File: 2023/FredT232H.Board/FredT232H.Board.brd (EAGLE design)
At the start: 88 x 77 mm, 17 parts

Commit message: Board 2023 fix first bug
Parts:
- moved LED_G_0 18.0 mm to (20.5, 47.0)
- moved LED_G_7 17.0 mm to (38.1, 47.0)
- moved LED_G_1 13.0 mm to (23.0, 47.0)
- moved LED_G_6 12.0 mm to (35.5, 47.0)
- moved LED_G_2 8.00 mm to (25.5, 47.0)
- moved LED_G_5 7.00 mm to (33.0, 47.0)
- moved LED_G_3 3.00 mm to (28.0, 47.0)
- moved LED_G_4 2.00 mm to (30.5, 47.0)
- moved GPIO_OUT 0.15 mm to (26.2, 15.3), turned to 180 degrees
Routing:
- net GND: track 233.4 -> 0.00 mm, vias 2 -> 0
- net VCC_33: track 168.6 -> 0.00 mm
- net D3_CS0: track 144.7 -> 0.00 mm
- net D4_CS1: track 108.8 -> 0.00 mm, vias 1 -> 0
- net D1_MOSI: track 107.8 -> 0.00 mm
- net D7_CS4: track 107.1 -> 0.00 mm, vias 1 -> 0
- net C4: track 105.8 -> 0.00 mm
- net D5_CS2: track 105.2 -> 0.00 mm, vias 1 -> 0
- net C7: track 103.8 -> 0.00 mm
- net D6_CS3: track 101.3 -> 0.00 mm, vias 2 -> 0
- net D2_MISO: track 99.5 -> 0.00 mm, vias 1 -> 0
- net D0_SCLK: track 98.9 -> 0.00 mm
- net C6: track 98.3 -> 0.00 mm
- net C5: track 92.8 -> 0.00 mm
- net C3: track 82.2 -> 0.00 mm
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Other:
- board text added: "PCBv2 - 2023.03"
- board text removed: "PCBv1 - 2023.02"

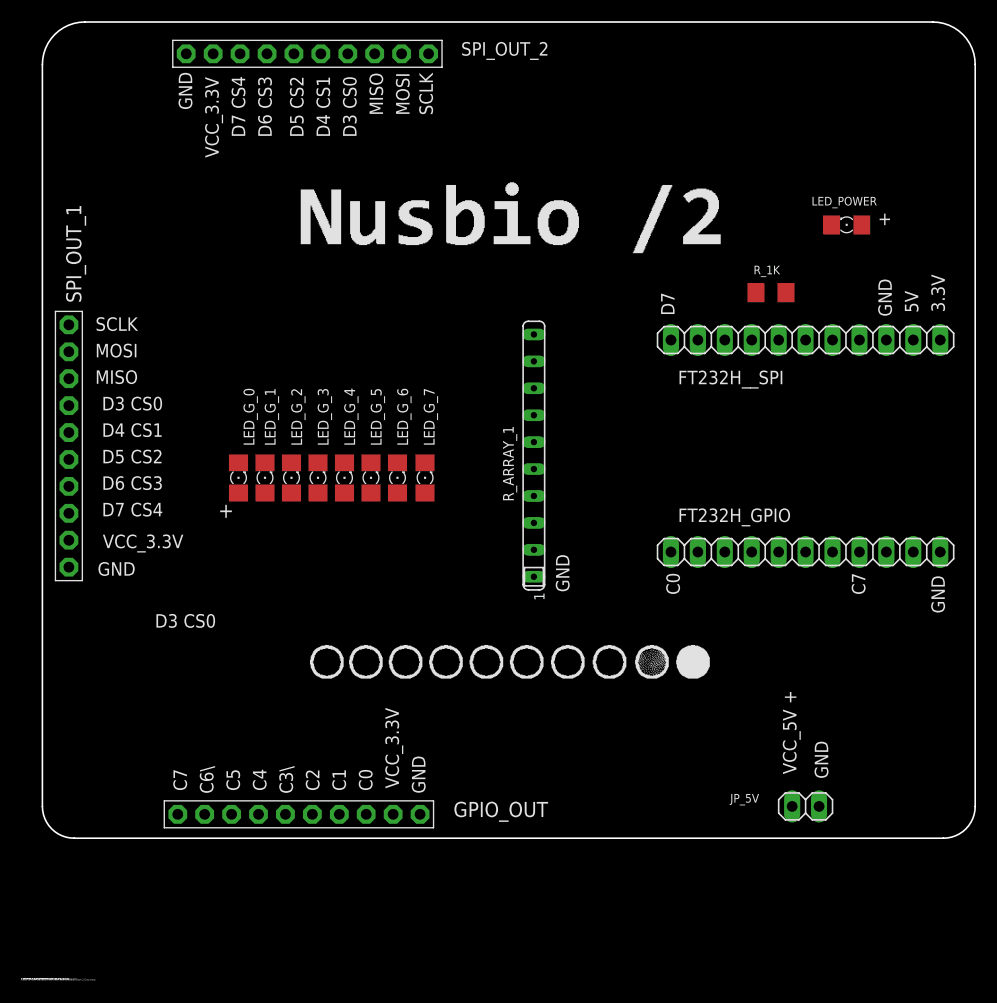
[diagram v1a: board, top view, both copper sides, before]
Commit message: Add pull up resistor to ft232h and i2c out 2
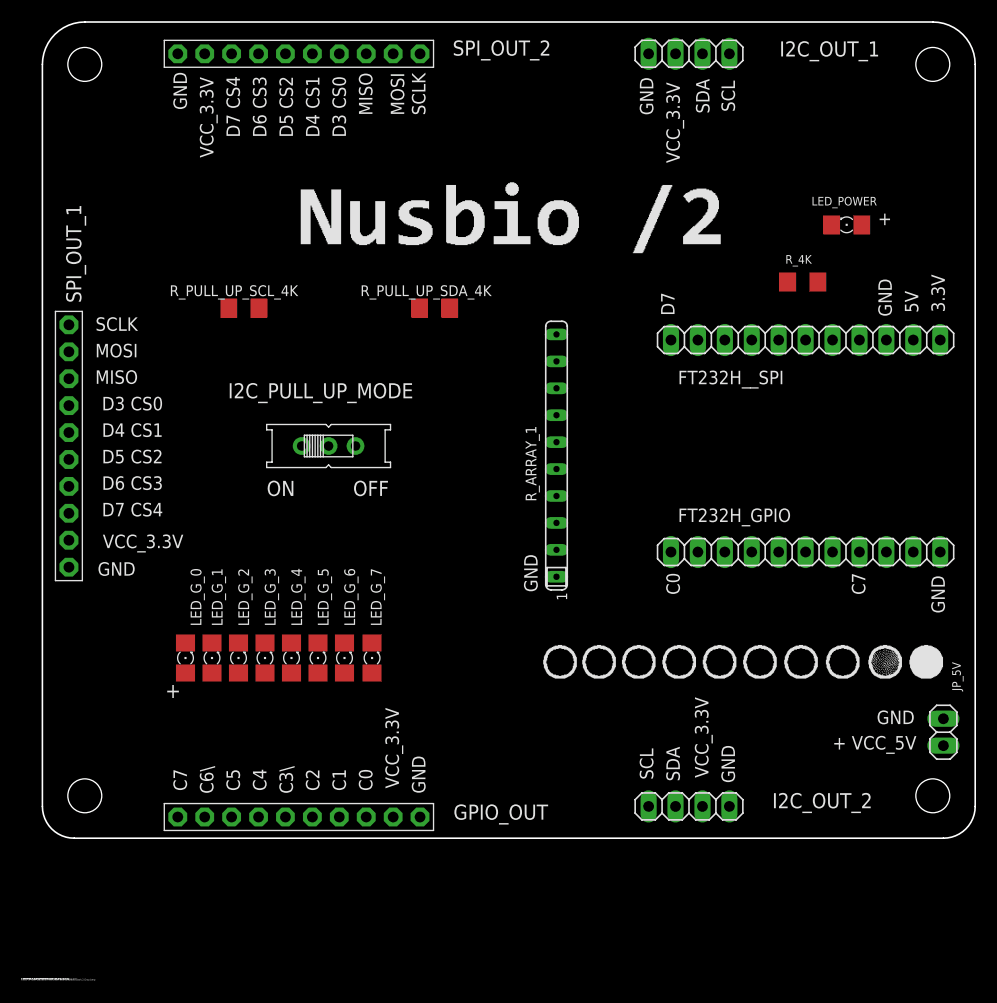
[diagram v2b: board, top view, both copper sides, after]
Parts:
- removed R_1K: (no value), adafruit:R1206
- added I2C_OUT_1, I2C_OUT_2: (no value), pinhead:1X04
- added I2C_PULL_UP_MODE: (no value), adafruit:EG1218
- added R_4K, R_PULL_UP_SCL_4K, R_PULL_UP_SDA_4K: (no value), adafruit:R1206
- moved LED_G_0 17.7 mm to (15.5, 30.0)
- moved LED_G_1 17.7 mm to (18.0, 30.0)
- moved LED_G_2 17.7 mm to (20.5, 30.0)
- moved LED_G_3 17.7 mm to (23.0, 30.0)
- moved LED_G_4 17.7 mm to (25.5, 30.0)
- moved LED_G_5 17.7 mm to (28.0, 30.0)
- moved LED_G_6 17.7 mm to (30.5, 30.0)
- moved LED_G_7 17.7 mm to (33.1, 30.0)
- moved JP_5V 14.8 mm to (87.0, 23.0), turned to 270 degrees
- moved R_ARRAY_1 2.13 mm to (50.5, 49.1)
- moved SPI_OUT_2 0.80 mm to (26.2, 87.0)
- moved GPIO_OUT 0.25 mm to (26.2, 15.0)
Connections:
- new net N$2: I2C_PULL_UP_MODE.O, R_PULL_UP_SCL_4K.2, R_PULL_UP_SDA_4K.2
- net D0_SCLK: now also I2C_OUT_1.1, I2C_OUT_2.1, R_PULL_UP_SCL_4K.1
- net D1_MOSI: now also R_PULL_UP_SDA_4K.1
- net D2_MISO: now also I2C_OUT_1.2, I2C_OUT_2.2
- net GND: now also I2C_OUT_1.4, I2C_OUT_2.4, R_4K.1; no longer R_1K.1
- net N$1: now also R_4K.2; no longer R_1K.2
- net VCC_33: now also I2C_OUT_1.3, I2C_OUT_2.3, I2C_PULL_UP_MODE.P
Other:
- board text added: "+ VCC_5V"
- board text added: "OFF"
- board text added: "ON"
- board text added: "SCL"
- board text added: "SDA"
- board text removed: "VCC_5V +"

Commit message: More on FT232 board
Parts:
- added H1, H2, H3, H4: MOUNT-PAD-ROUND3.3, holes:3,3-PAD
- added I2C_DTA_CONN: (no value), adafruit:EG1218
- moved JP_5V 53.0 mm to (87.0, 76.0)
- moved R_ARRAY_1 24.2 mm to (26.5, 52.1), turned to 270 degrees
- moved R_PULL_UP_SDA_4K 22.1 mm to (17.0, 65.0)
- moved I2C_PULL_UP_MODE 16.5 mm to (45.0, 54.0)
- moved R_PULL_UP_SCL_4K 16.1 mm to (37.0, 65.0)
- moved LED_G_0 4.24 mm to (18.5, 27.0)
- moved LED_G_1 4.24 mm to (21.0, 27.0)
- moved LED_G_2 4.24 mm to (23.5, 27.0)
- moved LED_G_3 4.24 mm to (26.0, 27.0)
- moved LED_G_4 4.24 mm to (28.5, 27.0)
- moved LED_G_5 4.24 mm to (31.0, 27.0)
- moved LED_G_6 4.24 mm to (33.5, 27.0)
- moved LED_G_7 4.24 mm to (36.1, 27.0)
- moved LED_POWER 2.00 mm to (75.9, 70.9)
- moved GPIO_OUT 0.50 mm to (26.2, 15.5)
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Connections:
- net D1_MOSI: now also I2C_DTA_CONN.P
- net D2_MISO: now also I2C_DTA_CONN.O
- net GND: now also H1.B3,3, H2.B3,3, H3.B3,3, H4.B3,3
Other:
- board text added: "VCC_3V"

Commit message: More on FT232 board
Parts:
- moved JP_5V 94.0 mm to (5.00, 30.0)
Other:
- board text added: "VCC_5V"
- board text removed: "+ VCC_5V"
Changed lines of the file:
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@@
 <text x="37.5" y="19" size="1.27" layer="25" rot="R90" align="center">GND</text>
 <text x="35" y="20.7" size="1.27" layer="25" rot="R90" align="center">VCC_3V</text>
-<text x="32.5" y="18.5" size="1.27" layer="25" rot="R90" align="center">C0</text>
-<text x="30" y="18.5" size="1.27" layer="25" rot="R90" align="center">C1</text>
-<text x="27.5" y="18.5" size="1.27" layer="25" rot="R90" align="center">C2</text>
-<text x="25" y="18.5" size="1.27" layer="25" rot="R90" align="center">C3\</text>
-<text x="22.5" y="18.5" size="1.27" layer="25" rot="R90" align="center">C4</text>
-<text x="20" y="18.5" size="1.27" layer="25" rot="R90" align="center">C5</text>
-<text x="17.5" y="18.5" size="1.27" layer="25" rot="R90" align="center">C6\</text>
-<text x="15" y="18.5" size="1.27" layer="25" rot="R90" align="center">C7</text>
+<text x="14.7" y="18.5" size="1.27" layer="25" rot="R90" align="center">C0</text>
+<text x="17.2" y="18.5" size="1.27" layer="25" rot="R90" align="center">C1</text>
+<text x="19.7" y="18.5" size="1.27" layer="25" rot="R90" align="center">C2</text>
+<text x="22.2" y="18.5" size="1.27" layer="25" rot="R90" align="center">C3\</text>
+<text x="24.8" y="18.5" size="1.27" layer="25" rot="R90" align="center">C4</text>
+<text x="27.5" y="18.5" size="1.27" layer="25" rot="R90" align="center">C5</text>
+<text x="30" y="18.5" size="1.27" layer="25" rot="R90" align="center">C6\</text>
+<text x="32.5" y="18.5" size="1.27" layer="25" rot="R90" align="center">C7</text>
 <text x="17.3255" y="23.939" size="1.4224" layer="25" rot="R180" align="center">+</text>
 <text x="0" y="-0.3175" size="0.127" layer="25" font="vector">C:/DVT/Fred.PCB/2023/MadeInTheUSB.Logo.Gray.50.bmp</text>
@@
 <text x="24.084" y="40.002" size="1.27" layer="25" rot="R90" align="center">GND</text>
 <text x="79" y="37" size="1.27" layer="25" rot="R270" align="center">C7</text>
-<text x="80.5" y="75" size="1.27" layer="25" align="center">+ VCC_5V</text>
-<text x="82.5" y="77.4" size="1.27" layer="25" align="center">GND</text>
+<text x="11" y="28.5" size="1.27" layer="25" align="center">VCC_5V</text>
+<text x="9.5" y="31.4" size="1.27" layer="25" align="center">GND</text>
 <text x="15" y="83.5" size="1.27" layer="25" rot="R90" align="center">GND</text>
 <text x="17.5" y="81" size="1.27" layer="25" rot="R90" align="center">VCC_3.3V</text>
@@
 <attribute name="VALUE" x="14.77" y="83.825" size="1.27" layer="27"/>
 </element>
-<element name="JP_5V" library="pinhead" library_urn="urn:adsk.eagle:library:325" package="1X02" package3d_urn="urn:adsk.eagle:package:22435/2" value="" x="87" y="76" smashed="yes" rot="R270">
-<attribute name="NAME" x="86.8288" y="72.6162" size="0.8128" layer="25" ratio="10" rot="R270"/>
-<attribute name="POPULARITY" value="98" x="87" y="76" size="1.778" layer="27" rot="R270" display="off"/>
-<attribute name="VALUE" x="83.825" y="78.54" size="1.27" layer="27" rot="R270"/>
+<element name="JP_5V" library="pinhead" library_urn="urn:adsk.eagle:library:325" package="1X02" package3d_urn="urn:adsk.eagle:package:22435/2" value="" x="5" y="30" smashed="yes" rot="R270">
+<attribute name="NAME" x="3.5" y="26" size="0.8128" layer="25" ratio="10"/>
+<attribute name="POPULARITY" value="98" x="5" y="30" size="1.778" layer="27" rot="R270" display="off"/>
+<attribute name="VALUE" x="1.825" y="32.54" size="1.27" layer="27" rot="R270"/>
 </element>
 <element name="I2C_OUT_1" library="pinhead" library_urn="urn:adsk.eagle:library:325" package="1X04" package3d_urn="urn:adsk.eagle:package:22407/2" value="" x="63" y="87" smashed="yes" rot="R180">
@@
 <contactref element="H3" pad="B3,3"/>
 <contactref element="H4" pad="B3,3"/>
-<wire x1="87" y1="77.27" x2="84" y2="84" width="0" layer="19" extent="1-1"/>
-<wire x1="81.62" y1="60" x2="87" y2="77.27" width="0" layer="19" extent="1-1"/>
-<wire x1="72.308" y1="65" x2="81.62" y2="60" width="0" layer="19" extent="1-1"/>
+<wire x1="72.308" y1="65" x2="84" y2="84" width="0" layer="19" extent="1-1"/>
+<wire x1="81.62" y1="60" x2="72.308" y2="65" width="0" layer="19" extent="1-1"/>
 <wire x1="86.7" y1="40" x2="81.62" y2="60" width="0" layer="19" extent="1-1"/>
 <wire x1="84" y1="19" x2="86.7" y2="40" width="0" layer="19" extent="1-1"/>
@@
 <wire x1="37.63" y1="15.5" x2="66.81" y2="15.5" width="0" layer="19" extent="1-1"/>
 <wire x1="8" y1="19" x2="37.63" y2="15.5" width="0" layer="19" extent="1-1"/>
-<wire x1="4.5" y1="38.57" x2="8" y2="19" width="0" layer="19" extent="1-1"/>
+<wire x1="5" y1="31.27" x2="8" y2="19" width="0" layer="19" extent="1-1"/>
+<wire x1="4.5" y1="38.57" x2="5" y2="31.27" width="0" layer="19" extent="1-1"/>
 <wire x1="26.5" y1="63.585" x2="4.5" y2="38.57" width="0" layer="19" extent="1-1"/>
 <wire x1="14.77" y1="87" x2="26.5" y2="63.585" width="0" layer="19" extent="1-1"/>
@@
 <contactref element="I2C_PULL_UP_MODE" pad="P"/>
 <contactref element="I2C_OUT_2" pad="3"/>
+<wire x1="86.7" y1="60" x2="61.73" y2="87" width="0" layer="19" extent="1-1"/>
 <wire x1="45" y1="54" x2="61.73" y2="87" width="0" layer="19" extent="1-1"/>
-<wire x1="86.7" y1="60" x2="61.73" y2="87" width="0" layer="19" extent="1-1"/>
 <wire x1="35.09" y1="15.5" x2="45" y2="54" width="0" layer="19" extent="1-1"/>
 <wire x1="64.27" y1="15.5" x2="35.09" y2="15.5" width="0" layer="19" extent="1-1"/>
@@
 <contactref element="LED_POWER" pad="A"/>
 <contactref element="JP_5V" pad="2"/>
-<wire x1="77.298134375" y1="70.86644375" x2="87" y2="74.73" width="0" layer="19" extent="1-1"/>
 <wire x1="84.16" y1="60" x2="77.298134375" y2="70.86644375" width="0" layer="19" extent="1-1"/>
+<wire x1="5" y1="28.73" x2="77.298134375" y2="70.86644375" width="0" layer="19" extent="1-1"/>
 </signal>
 <signal name="D0_SCLK">
@@
 <wire x1="37.63" y1="87" x2="66.81" y2="87" width="0" layer="19" extent="1-1"/>
 <wire x1="35.578" y1="65" x2="37.63" y2="87" width="0" layer="19" extent="1-1"/>
+<wire x1="79.08" y1="60" x2="66.81" y2="87" width="0" layer="19" extent="1-1"/>
 <wire x1="4.5" y1="61.43" x2="35.578" y2="65" width="0" layer="19" extent="1-1"/>
-<wire x1="79.08" y1="60" x2="66.81" y2="87" width="0" layer="19" extent="1-1"/>
 <wire x1="59.19" y1="15.5" x2="79.08" y2="60" width="0" layer="19" extent="1-1"/>
 </signal>
@@
 <wire x1="45" y1="44.5" x2="76.54" y2="60" width="0" layer="19" extent="1-1"/>
 <wire x1="15.578" y1="65" x2="45" y2="44.5" width="0" layer="19" extent="1-1"/>
+<wire x1="4.5" y1="58.89" x2="15.578" y2="65" width="0" layer="19" extent="1-1"/>
 <wire x1="35.09" y1="87" x2="15.578" y2="65" width="0" layer="19" extent="1-1"/>
-<wire x1="4.5" y1="58.89" x2="15.578" y2="65" width="0" layer="19" extent="1-1"/>
 </signal>
 <signal name="D2_MISO">
@@
 <contactref element="R_ARRAY_1" pad="8"/>
 <contactref element="LED_G_6" pad="C"/>
-<wire x1="26.5" y1="45.805" x2="33.5" y2="28.422" width="0" layer="19" extent="1-1"/>
+<wire x1="33.5" y1="28.422" x2="26.5" y2="45.805" width="0" layer="19" extent="1-1"/>
 </signal>
 <signal name="R_G_7">
 <contactref element="R_ARRAY_1" pad="9"/>
 <contactref element="LED_G_7" pad="C"/>
-<wire x1="26.5" y1="43.265" x2="36.101209375" y2="28.422" width="0" layer="19" extent="1-1"/>
+<wire x1="36.101209375" y1="28.422" x2="26.5" y2="43.265" width="0" layer="19" extent="1-1"/>
 </signal>
 <signal name="N$2">
@@
 <contactref element="R_PULL_UP_SCL_4K" pad="2"/>
 <contactref element="I2C_PULL_UP_MODE" pad="O"/>
-<wire x1="42.46" y1="54" x2="18.422" y2="65" width="0" layer="19" extent="1-1"/>
-<wire x1="38.422" y1="65" x2="18.422" y2="65" width="0" layer="19" extent="1-1"/>
+<wire x1="42.46" y1="54" x2="38.422" y2="65" width="0" layer="19" extent="1-1"/>
+<wire x1="18.422" y1="65" x2="38.422" y2="65" width="0" layer="19" extent="1-1"/>
 </signal>
 </signals>
